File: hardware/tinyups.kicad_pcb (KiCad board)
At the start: 4 copper layers, 150 x 140 mm, 124 parts, among them J1 XT60, J2 XT30, J3 USB, J4 SWD, J5 FAN, J6 PACK, J7 CELLS, Q1 N-FET 40V, Q10 N-FET 40V, Q11 N-FET 40V, Q12 N-FET 40V, Q2 N-FET 40V, Q3 N-FET 30V, Q4 N-FET 30V, Q5 N-FET 30V, Q6 N-FET 30V, Q7 N-FET 40V, Q8 N-FET 40V, Q9 N-FET 40V, U1 LM5069, U2 LM74700-Q1, U3 BQ25720, U4 LM5176, U5 BQ76942, U6 RP2040, U7 W25Q128, U8 3V3, Y1 12MHz

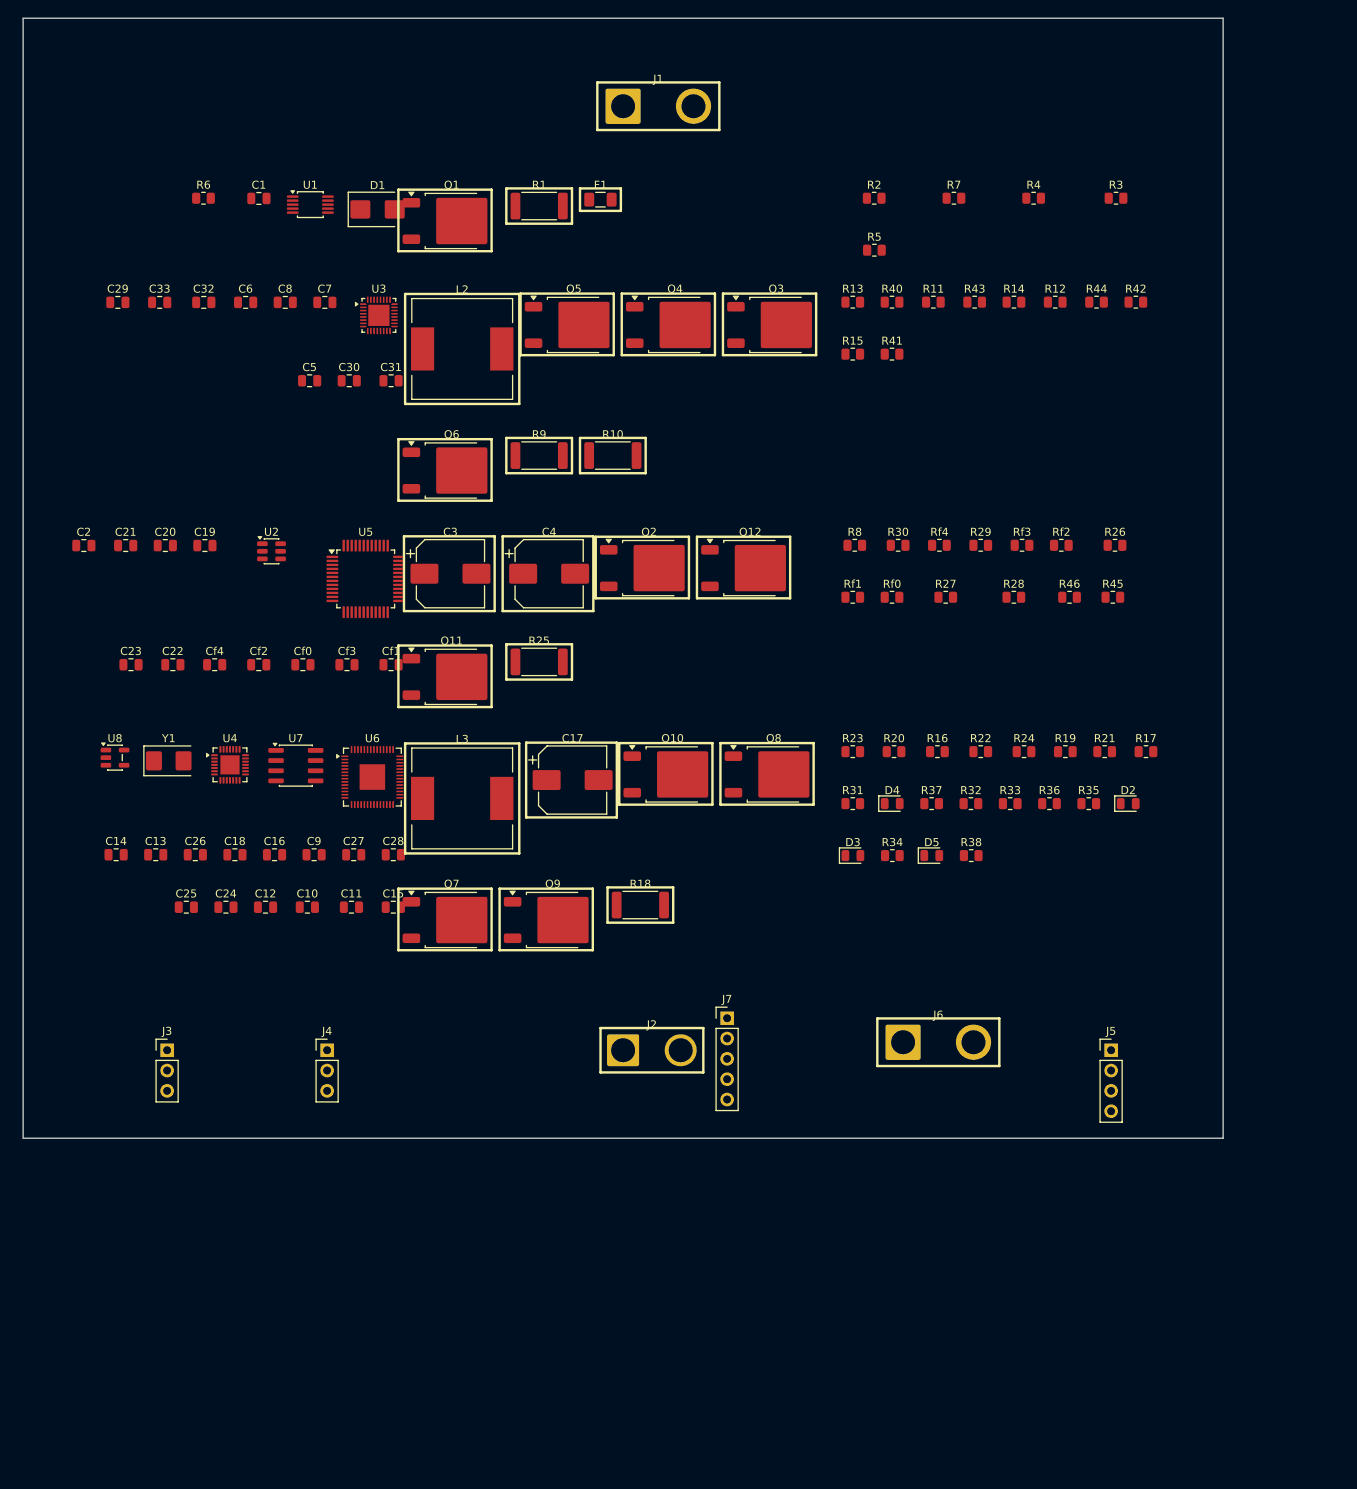
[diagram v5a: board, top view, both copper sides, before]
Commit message: try to find a new placement approach
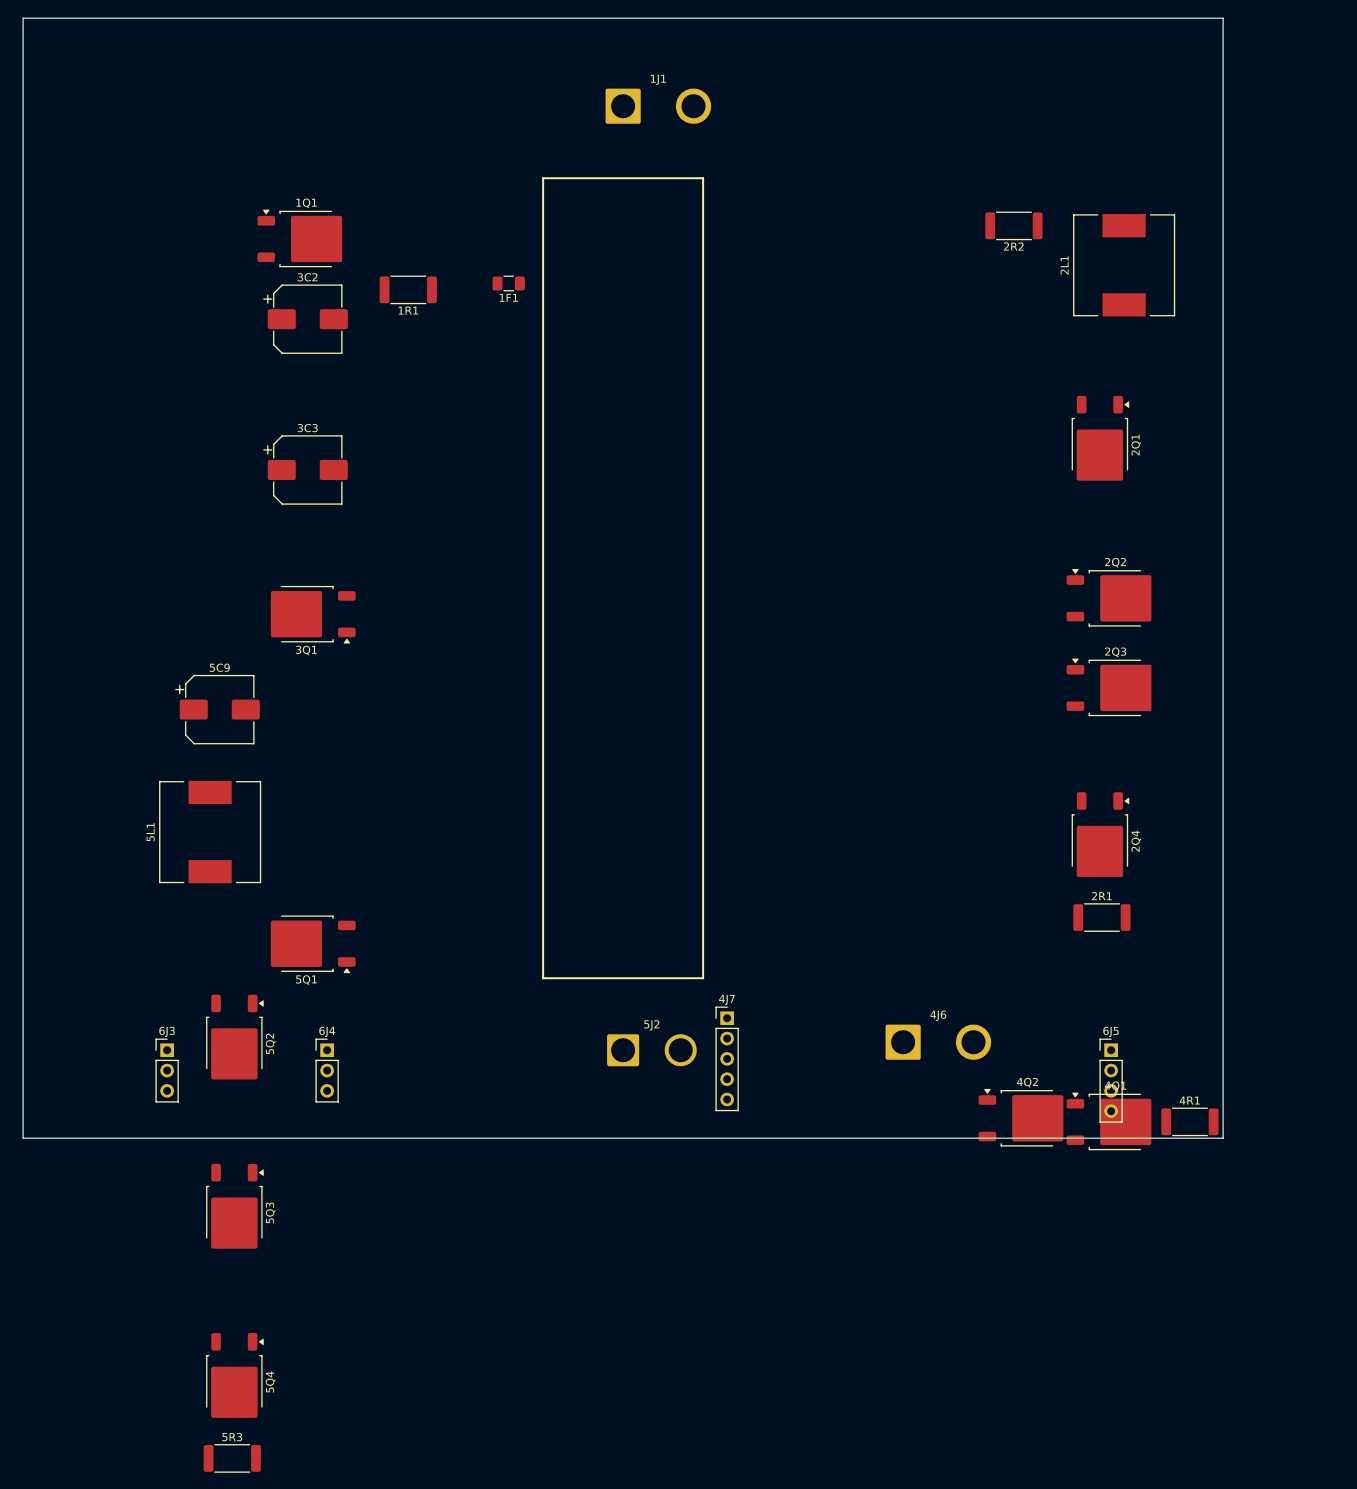
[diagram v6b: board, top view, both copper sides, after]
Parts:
- removed C1: TBD, Capacitor_SMD:C_0805_2012Metric
- removed C10, C11, C2, C23, C31, C32, C33, Cf0, Cf1, Cf2, Cf3, Cf4: 100n, Capacitor_SMD:C_0805_2012Metric
- removed C12, C29: 10n, Capacitor_SMD:C_0805_2012Metric
- removed C13, C14, C15, C30: 1n, Capacitor_SMD:C_0805_2012Metric
- removed C16, C19, C20, C21, C22, C28, C7, C8: 1u, Capacitor_SMD:C_0805_2012Metric
- removed C17: 220u, Capacitor_SMD:CP_Elec_8x10
- removed C18, C26, C27, C9: 10u, Capacitor_SMD:C_0805_2012Metric
- removed C24, C25: 20p, Capacitor_SMD:C_0805_2012Metric
- removed C3, C4: 470u, Capacitor_SMD:CP_Elec_8x10
- removed C5, C6: 47n, Capacitor_SMD:C_0805_2012Metric
- removed D1: SMBJ15A, Diode_SMD:D_SMB
- removed D2, D3, D4, D5: LED, LED_SMD:LED_0805_2012Metric
- removed F1: 25A, Fuse:Fuse_1206_3216Metric
- removed J1: XT60, Connector_Wire:SolderWire-2.5sqmm_1x02_P8.8mm_D2.4mm_OD4.4mm
- removed J2: XT30, Connector_Wire:SolderWire-2.5sqmm_1x02_P7.2mm_D2.4mm_OD3.6mm
- removed J3: USB, Connector_PinHeader_2.54mm:PinHeader_1x03_P2.54mm_Vertical
- removed J4: SWD, Connector_PinHeader_2.54mm:PinHeader_1x03_P2.54mm_Vertical
- removed J5: FAN, Connector_PinHeader_2.54mm:PinHeader_1x04_P2.54mm_Vertical
- removed J6: PACK, Connector_Wire:SolderWire-2.5sqmm_1x02_P8.8mm_D2.4mm_OD4.4mm
- removed J7: CELLS, Connector_PinHeader_2.54mm:PinHeader_1x05_P2.54mm_Vertical
- removed L2: 2.2u, Inductor_SMD:L_12x12mm_H8mm
- removed L3: 1u0, Inductor_SMD:L_12x12mm_H8mm
- removed Q1, Q10, Q11, Q12, Q2, Q7, Q8, Q9: N-FET 40V, Package_TO_SOT_SMD:TO-252-2
- removed Q3, Q4, Q5, Q6: N-FET 30V, Package_TO_SOT_SMD:TO-252-2
- removed R1: 2.2m, Resistor_SMD:R_2512_6332Metric
- removed R10, R9: 5m, Resistor_SMD:R_2512_6332Metric
- removed R11, R12, R16, R22, R24, R29, R30, R45, R46, R8: 100k, Resistor_SMD:R_0805_2012Metric
- removed R13, R14, R15, R21, R23, R38, R40, R41, R42, R43, R44: 10k, Resistor_SMD:R_0805_2012Metric
- removed R17: 7k15, Resistor_SMD:R_0805_2012Metric
- removed R18, R25: 1m, Resistor_SMD:R_2512_6332Metric
- removed R19: 27k, Resistor_SMD:R_0805_2012Metric
- removed R2: TBD-UV-hi, Resistor_SMD:R_0805_2012Metric
- removed R20: 93k1, Resistor_SMD:R_0805_2012Metric
- removed R26, R27, R28: 10k-NTC, Resistor_SMD:R_0805_2012Metric
- removed R3: TBD-UV-lo, Resistor_SMD:R_0805_2012Metric
- removed R31, R32, R33, R34, R35: 1k, Resistor_SMD:R_0805_2012Metric
- removed R36, R37: 27, Resistor_SMD:R_0805_2012Metric
- removed R4: TBD-OV-hi, Resistor_SMD:R_0805_2012Metric
- removed R5: TBD-OV-lo, Resistor_SMD:R_0805_2012Metric
- removed R6: TBD-PWR, Resistor_SMD:R_0805_2012Metric
- removed R7: 100k-PGD, Resistor_SMD:R_0805_2012Metric
- removed Rf0, Rf1, Rf2, Rf3, Rf4: 100, Resistor_SMD:R_0805_2012Metric
- removed U1: LM5069, Package_SO:VSSOP-10_3x3mm_P0.5mm
- removed U2: LM74700-Q1, Package_TO_SOT_SMD:SOT-23-6
- removed U3: BQ25720, Package_DFN_QFN:QFN-32-1EP_4x4mm_P0.4mm_EP2.65x2.65mm
- removed U4: LM5176, Package_DFN_QFN:QFN-28-1EP_4x4mm_P0.4mm_EP2.4x2.4mm
- removed U5: BQ76942, Package_QFP:TQFP-48_7x7mm_P0.5mm
- removed U6: RP2040, Package_DFN_QFN:QFN-56-1EP_7x7mm_P0.4mm_EP3.2x3.2mm
- removed U7: W25Q128, Package_SO:SOIC-8_3.9x4.9mm_P1.27mm
- removed U8: 3V3, Package_TO_SOT_SMD:SOT-23-5
- removed Y1: 12MHz, Crystal:Crystal_SMD_5032-2Pin_5.0x3.2mm
- added 1F1: 25A, Fuse:Fuse_1206_3216Metric, F.Cu at (60.7, 33.2)
- added 1J1: XT60, Connector_Wire:SolderWire-2.5sqmm_1x02_P8.8mm_D2.4mm_OD4.4mm, F.Cu at (75.0, 11.0)
- added 1Q1: N-FET 40V, Package_TO_SOT_SMD:TO-252-2, F.Cu at (35.4, 27.6)
- added 1R1: 2.2m, Resistor_SMD:R_2512_6332Metric, F.Cu at (48.1, 34.0)
- added 2L1: 2.2u, Inductor_SMD:L_12x12mm_H8mm, F.Cu at (137.6, 30.9)
- added 2Q1: N-FET 30V, Package_TO_SOT_SMD:TO-252-2, F.Cu at (134.6, 53.3)
- added 2Q2: N-FET 30V, Package_TO_SOT_SMD:TO-252-2, F.Cu at (136.6, 72.5)
- added 2Q3: N-FET 30V, Package_TO_SOT_SMD:TO-252-2, F.Cu at (136.6, 83.7)
- added 2Q4: N-FET 30V, Package_TO_SOT_SMD:TO-252-2, F.Cu at (134.6, 102.9)
- added 2R1: 5m, Resistor_SMD:R_2512_6332Metric, F.Cu at (134.9, 112.4)
- added 2R2: 5m, Resistor_SMD:R_2512_6332Metric, F.Cu at (123.9, 26.0)
- added 3C2: 470u, Capacitor_SMD:CP_Elec_8x10, F.Cu at (35.6, 37.6)
- added 3C3: 470u, Capacitor_SMD:CP_Elec_8x10, F.Cu at (35.6, 56.5)
- added 3Q1: N-FET 40V, Package_TO_SOT_SMD:TO-252-2, F.Cu at (35.4, 74.5)
- added 4J6: PACK, Connector_Wire:SolderWire-2.5sqmm_1x02_P8.8mm_D2.4mm_OD4.4mm, F.Cu at (110.0, 128.0)
- added 4J7: CELLS, Connector_PinHeader_2.54mm:PinHeader_1x05_P2.54mm_Vertical, F.Cu at (88.0, 125.0)
- added 4Q1: N-FET 40V, Package_TO_SOT_SMD:TO-252-2, F.Cu at (136.6, 138.0)
- added 4Q2: N-FET 40V, Package_TO_SOT_SMD:TO-252-2, F.Cu at (125.6, 137.5)
- added 4R1: 1m, Resistor_SMD:R_2512_6332Metric, F.Cu at (145.9, 138.0)
- added 5C9: 220u, Capacitor_SMD:CP_Elec_8x10, F.Cu at (24.6, 86.4)
- added 5J2: XT30, Connector_Wire:SolderWire-2.5sqmm_1x02_P7.2mm_D2.4mm_OD3.6mm, F.Cu at (75.0, 129.0)
- added 5L1: 1u0, Inductor_SMD:L_12x12mm_H8mm, F.Cu at (23.4, 101.7)
- added 5Q1: N-FET 40V, Package_TO_SOT_SMD:TO-252-2, F.Cu at (35.4, 115.7)
- added 5Q2: N-FET 40V, Package_TO_SOT_SMD:TO-252-2, F.Cu at (26.4, 128.2)
- added 5Q3: N-FET 40V, Package_TO_SOT_SMD:TO-252-2, F.Cu at (26.4, 149.3)
- added 5Q4: N-FET 40V, Package_TO_SOT_SMD:TO-252-2, F.Cu at (26.4, 170.5)
- added 5R3: 1m, Resistor_SMD:R_2512_6332Metric, F.Cu at (26.1, 180.0)
- added 6J3: USB, Connector_PinHeader_2.54mm:PinHeader_1x03_P2.54mm_Vertical, F.Cu at (18.0, 129.0)
- added 6J4: SWD, Connector_PinHeader_2.54mm:PinHeader_1x03_P2.54mm_Vertical, F.Cu at (38.0, 129.0)
- added 6J5: FAN, Connector_PinHeader_2.54mm:PinHeader_1x04_P2.54mm_Vertical, F.Cu at (136.0, 129.0)
